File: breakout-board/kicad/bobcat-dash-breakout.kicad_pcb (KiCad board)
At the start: 2 copper layers, 162 x 159 mm, 169 parts, among them J1 TO PI (40-pin ribbon), J10 ADS1115 PWR/I2C, J11 LIGHTS, J12 COIL, J13 TILT, J14 TEMP PROBE, J15 ADS1115 INPUTS, J16 MAX98357A STEREO, J2 POWER IN, J3 TO 5V BUCK, J4 SWITCHES, J5 TACH, J6 FUEL, J7 HORN, J8 SILENCE, J9 MAX98357A MONO, Q1 IRLZ44N, Q2 IRF4905, Q3 BC547B, Q4 BC547B, U1 PC817, U10 PC817, U11 DS18B20, U4 PC817, U5 PC817, U6 CD4060BE, U7 PC817, U8 PC817, U9 PC817

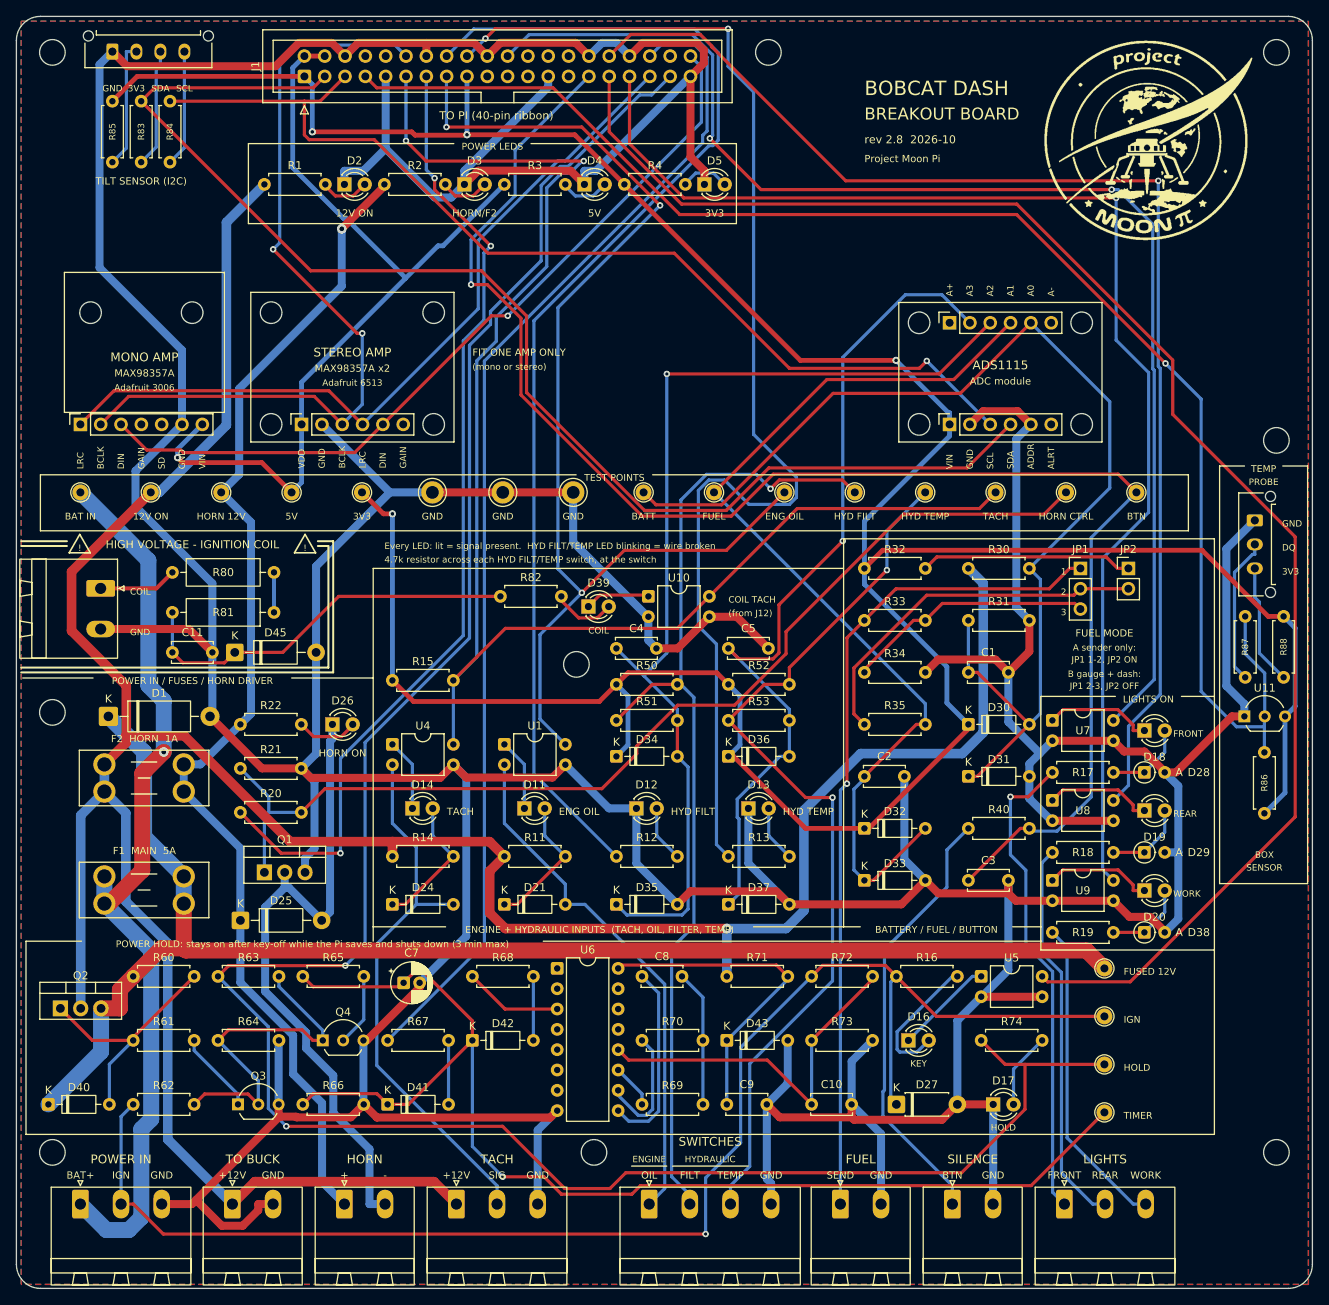
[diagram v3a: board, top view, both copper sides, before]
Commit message: S.S.O.M.S: menu screens, service reminders, service Wi-Fi web page, USB stick, board rev 2.9, button pod
Dash (now S.S.O.M.S, System Status, Operations, and Maintenance System; Bobcat M700):
- Menu buttons and screens: HISTORY (clear one / all, ALL ALARMS archive), SERVICE (Bobcat 700 schedule,
  climate setting, details, mark done), SYSTEM; alarms lock the menus until SILENCE; pod fan control.
- Service Wi-Fi (SYSTEM > OK): hotspot + built-in web page (status, performance reports, alarms, service,
  downloads, software update / go back); 30 min countdown, EXTEND on the web page, off at key-off;
  connected devices shown on the dash.
- Usage recording for the reports: full throttle / part throttle / idle / overspeed, starts, hot shutdowns,
  temperatures; day-by-day table paged in the browser (10/20/50/100).
- USB stick: copies the reports and a data backup, offers updates found on the stick.
- Maintenance code (set at first use, no repeated or sequential digits, lockout, recovery code, SD card
  reset-code file): service Wi-Fi, USB install, clearing alarms, marking service done, and the web page's
  install / go back / restart.
- E-BOX (electronics box) temperature naming; S.S.O.M.S splash caption and header.

Breakout board rev 2.9: button pod plug J17 (4 menu buttons, SILENCE, 12 V pod fan via Q5), routed and
DRC clean. route.py shuffles the net order per attempt (Freerouting is deterministic). The generator
also has the next layout change (TILT plug under the E-BOX sensor, new title, edge border), not yet routed.

Button pod enclosure (enclosure/button-pod): Eaton M22 buttons, Pi inside, bolt-on arm and gusset.

Co-Authored-By: Claude Opus 5.5 <noreply@anthropic.com>
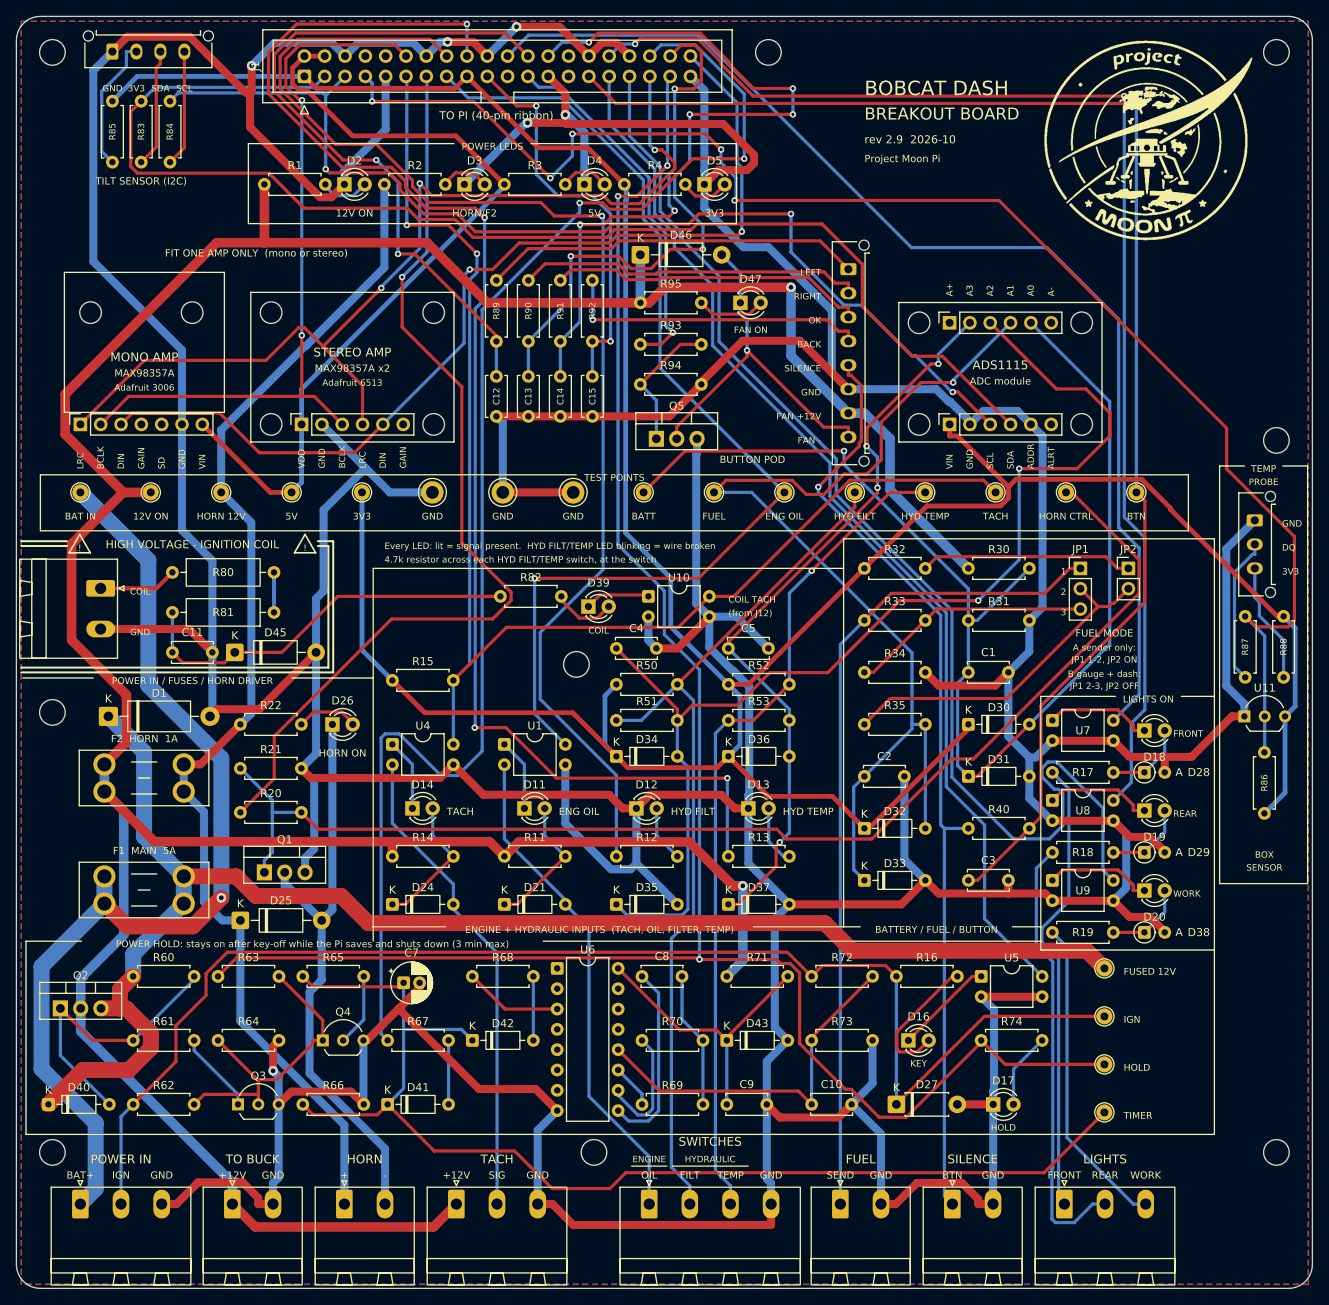
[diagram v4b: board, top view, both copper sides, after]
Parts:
- added C12: 100nF, Capacitor_THT:C_Disc_D5.0mm_W2.5mm_P5.00mm, F.Cu at (60.0, 45.0)
- added C13: 100nF, Capacitor_THT:C_Disc_D5.0mm_W2.5mm_P5.00mm, F.Cu at (64.0, 45.0)
- added C14: 100nF, Capacitor_THT:C_Disc_D5.0mm_W2.5mm_P5.00mm, F.Cu at (68.0, 45.0)
- added C15: 100nF, Capacitor_THT:C_Disc_D5.0mm_W2.5mm_P5.00mm, F.Cu at (72.0, 45.0)
- added D46: 1N4007, Diode_THT:D_DO-41_SOD81_P10.16mm_Horizontal, F.Cu at (78.0, 29.8)
- added D47: LED_green, LED_THT:LED_D3.0mm, F.Cu at (90.5, 35.8)
- added J17: POD, Connector_Molex:Molex_Micro-Fit_3.0_43650-0815_1x08_P3.00mm_Vertical, F.Cu at (104.0, 31.6)
- added Q5: IRLZ44N, Package_TO_SOT_THT:TO-220-3_Vertical, F.Cu at (80.0, 52.8)
- added R89: 1k, Resistor_THT:R_Axial_DIN0207_L6.3mm_D2.5mm_P7.62mm_Horizontal, F.Cu at (60.0, 33.0)
- added R90: 1k, Resistor_THT:R_Axial_DIN0207_L6.3mm_D2.5mm_P7.62mm_Horizontal, F.Cu at (64.0, 33.0)
- added R91: 1k, Resistor_THT:R_Axial_DIN0207_L6.3mm_D2.5mm_P7.62mm_Horizontal, F.Cu at (68.0, 33.0)
- added R92: 1k, Resistor_THT:R_Axial_DIN0207_L6.3mm_D2.5mm_P7.62mm_Horizontal, F.Cu at (72.0, 33.0)
- added R93: 100, Resistor_THT:R_Axial_DIN0207_L6.3mm_D2.5mm_P7.62mm_Horizontal, F.Cu at (78.0, 41.0)
- added R94: 10k, Resistor_THT:R_Axial_DIN0207_L6.3mm_D2.5mm_P7.62mm_Horizontal, F.Cu at (78.0, 46.0)
- added R95: 3.3k, Resistor_THT:R_Axial_DIN0207_L6.3mm_D2.5mm_P7.62mm_Horizontal, F.Cu at (78.0, 35.8)
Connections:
- net Net-(J8-Pin_1) renamed BTN_IN
- J1 pad 19: unconnected-(J1-Pin_19-Pad19) -> BTN_BACK_GPIO
- J1 pad 23: unconnected-(J1-Pin_23-Pad23) -> FAN_GPIO
- J1 pad 24: unconnected-(J1-Pin_24-Pad24) -> BTN_L_GPIO
- J1 pad 26: unconnected-(J1-Pin_26-Pad26) -> BTN_R_GPIO
- J1 pad 38: unconnected-(J1-Pin_38-Pad38) -> BTN_OK_GPIO
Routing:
- net GND: track 1026.8 -> 1189.0 mm, vias 0 -> 6
- net BTN_R_GPIO: track 0.00 -> 105.4 mm, vias 0 -> 6
- net BTN_L_GPIO: track 0.00 -> 89.4 mm, vias 0 -> 2
- net BTN_IN: track 55.0 -> 117.9 mm, vias 0 -> 1
- net BTN_OK_GPIO: track 0.00 -> 60.6 mm, vias 0 -> 3
- net KEY_GPIO: track 193.1 -> 134.9 mm
- net BTN_BACK_GPIO: track 0.00 -> 50.1 mm, vias 0 -> 2
- net BTN_L_IN: track 0.00 -> 47.5 mm
- net FAN_DRAIN: track 0.00 -> 45.9 mm, vias 0 -> 1
- net FAN_GPIO: track 0.00 -> 45.7 mm, vias 0 -> 1
- net BTN_R_IN: track 0.00 -> 43.3 mm
- net HOLD_GPIO: track 290.1 -> 249.2 mm, vias 2 -> 3
- net BTN_OK_IN: track 0.00 -> 40.0 mm
- net +12V: track 377.8 -> 417.2 mm, vias 1 -> 2
- net BTN_BACK_IN: track 0.00 -> 38.7 mm, vias 0 -> 1
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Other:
- board text added: "BACK"
- board text added: "BUTTON POD"
- board text added: "FAN +12V"
- board text added: "FAN -"
- board text added: "FAN ON"
- board text added: "FIT ONE AMP ONLY (mono or stereo)"
- board text added: "LEFT"
- board text added: "OK"
- board text added: "RIGHT"
- board text added: "rev 2.9 2026-10"
- board text removed: "(mono or stereo)"
- board text removed: "FIT ONE AMP ONLY"
- board text removed: "rev 2.8 2026-10"

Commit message: M.O.S.S. rename, settings, B612 font, board rev 2.9 layout (blue, 0.6 mm supplies)
Software:
- System renamed M.O.S.S. (Maintenance, Operations, and Service System);
  Wi-Fi SSID and USB folder MOSS-BOBCAT-M700
- Maintenance code: lockout, recovery code, SD-card reset; gates clears,
  mark done, clock, Wi-Fi, USB and web install/restore/restart;
  "are you sure?" pop-ups default to NO
- Settings: C/F units, 12h/24h clock, set clock (device sync / by hand on
  web or dash), named time zone with automatic DST
- Web: status tiles (engine status links to service/alarms), Wi-Fi EXTEND,
  reports with daily temp/battery charts, extremes with time, paged day
  table, throttle bands reframed; alarm durations to the second
- B612 font on the dash and web; BOX renamed E-BOX

Board rev 2.9:
- TILT plug level with the ADC module, TEMP column 7 mm lower, H18 moved
- +3V3 and +5V at 0.6 mm, signals 0.3 mm / 0.25 mm, 0.8 mm edge keepout
- Blue solder mask (main board and ADS1115 adapter); routed, DRC clean
- adapter/ renamed ads1115-adapter/; diagrams and BOM moved to docs/

Co-Authored-By: Claude Opus 5.5 <noreply@anthropic.com>
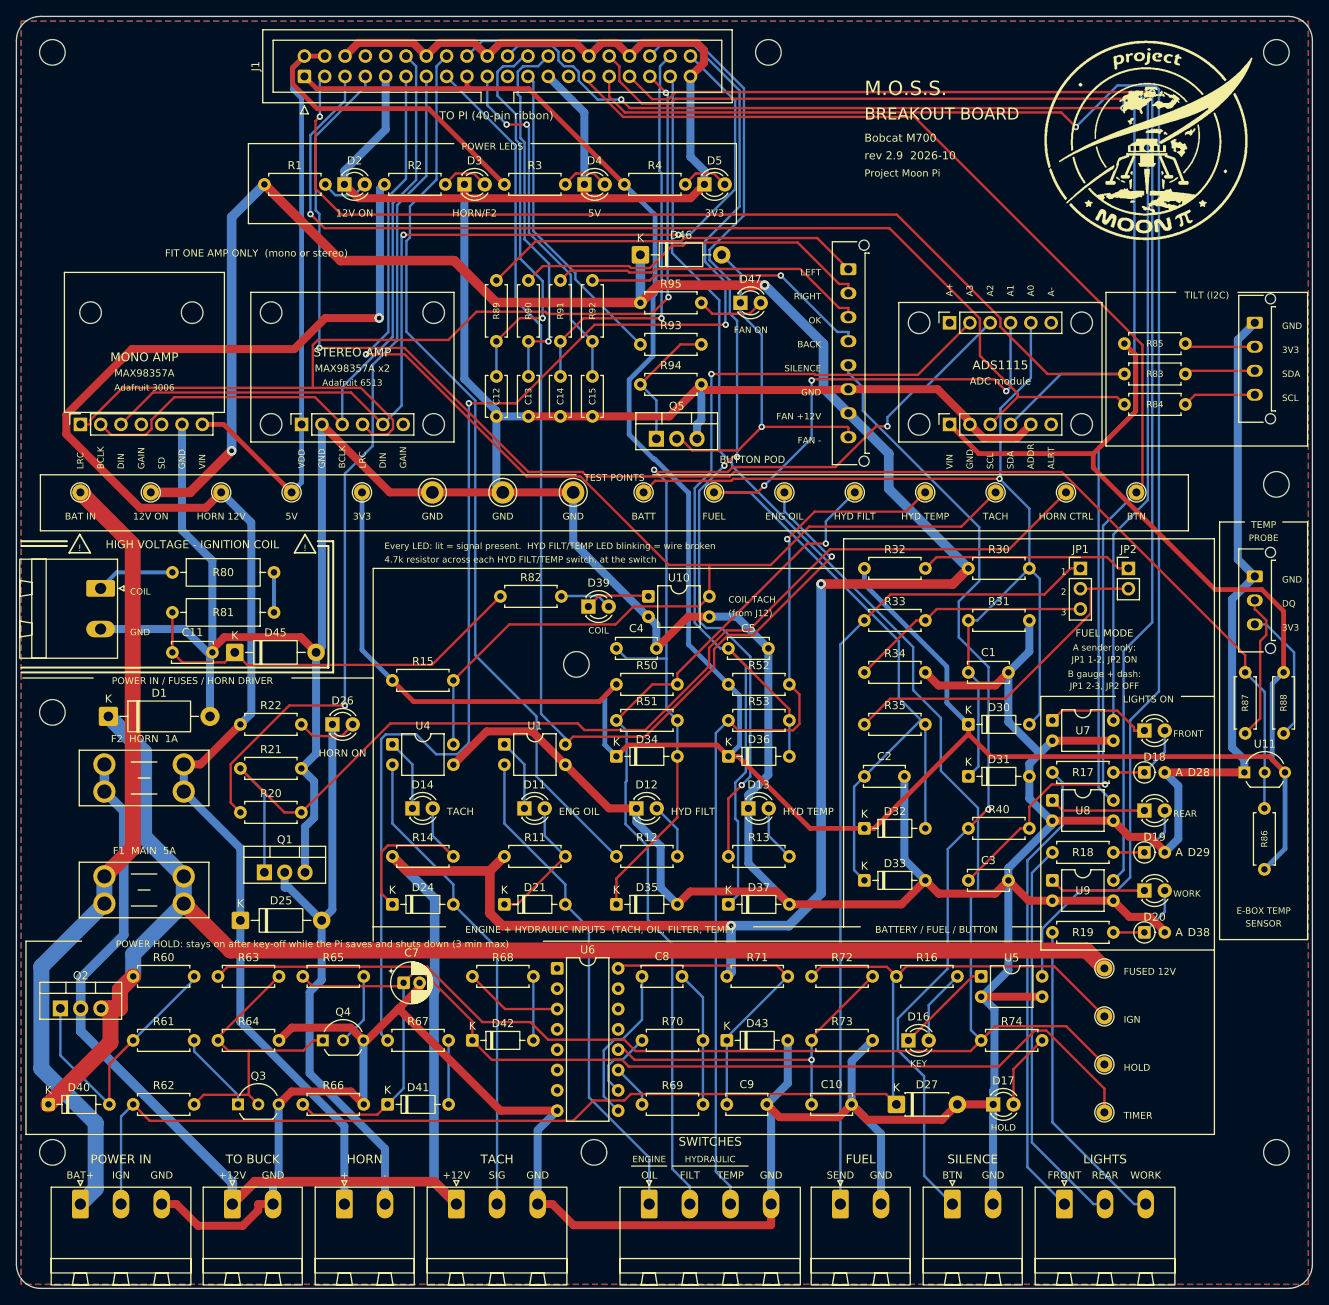
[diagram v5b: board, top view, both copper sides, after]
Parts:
- moved J13 146.8 mm to (154.8, 38.3), turned to -90 degrees
- moved R85 130.1 mm to (138.5, 40.9), turned to 0 degrees
- moved R83 127.5 mm to (138.5, 44.7), turned to 0 degrees
- moved R84 125.2 mm to (138.5, 48.5), turned to 0 degrees
- moved J14 7.00 mm to (154.8, 70.0)
- moved R86 7.00 mm to (156.0, 99.0)
- moved R87 7.00 mm to (153.6, 82.0)
- moved R88 7.00 mm to (158.4, 82.0)
- moved U11 7.00 mm to (153.5, 94.5)
- moved H18 5.50 mm to (157.5, 58.5)
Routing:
- net GND: track 1189.0 -> 1058.4 mm, vias 6 -> 0
- net KEY_GPIO: track 134.9 -> 194.8 mm, vias 0 -> 1
- net BTN_R_GPIO: track 105.4 -> 46.9 mm, vias 6 -> 1
- net FILT_LED: track 161.2 -> 113.0 mm, vias 1 -> 0
- net BTN_L_GPIO: track 89.4 -> 49.1 mm, vias 2 -> 1
- net +12V_HORN: track 151.9 -> 191.0 mm, vias 0 -> 1
- net TEMP_LED: track 177.6 -> 144.2 mm, vias 4 -> 3
- net TEMP_ADC: track 93.9 -> 123.3 mm, vias 4 -> 1
- net FILT_ADC: track 144.1 -> 116.0 mm
- net BATT_ADC: track 154.5 -> 130.5 mm
- net +12V: track 417.2 -> 441.0 mm, vias 2 -> 4
- net +12V_IN: track 123.1 -> 100.0 mm, vias 1 -> 0
- net LT_FRONT_GPIO: track 144.7 -> 166.0 mm, vias 0 -> 2
- net +3V3: track 398.3 -> 418.2 mm
- net SDA: track 160.7 -> 142.7 mm, vias 0 -> 1
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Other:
- board text added: "Bobcat M700"
- board text added: "E-BOX TEMP"
- board text added: "M.O.S.S."
- board text added: "TILT (I2C)"
- board text removed: "BOBCAT DASH"
- board text removed: "BOX"
- board text removed: "TILT SENSOR (I2C)"
